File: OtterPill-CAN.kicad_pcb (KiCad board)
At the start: 2 copper layers, 30.7 x 17.6 mm, 10 parts, among them J1 pinh, J2 pinh, J3 CAN, J5 SWD, J7 PAD, U1 TJA1051T-3

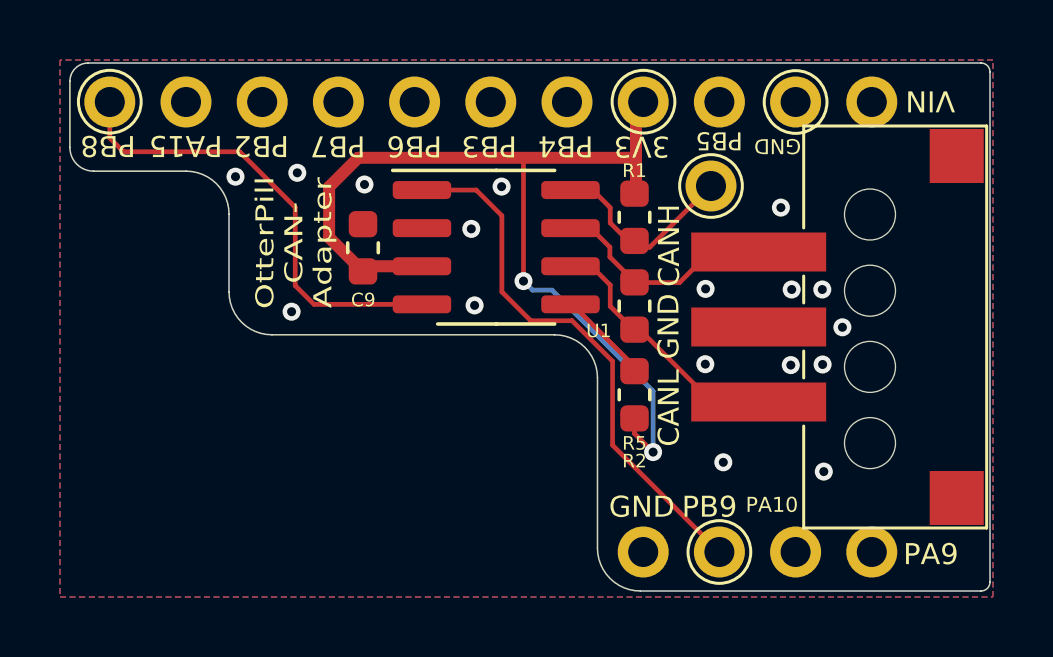
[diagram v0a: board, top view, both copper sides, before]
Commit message: updated to kicad 6
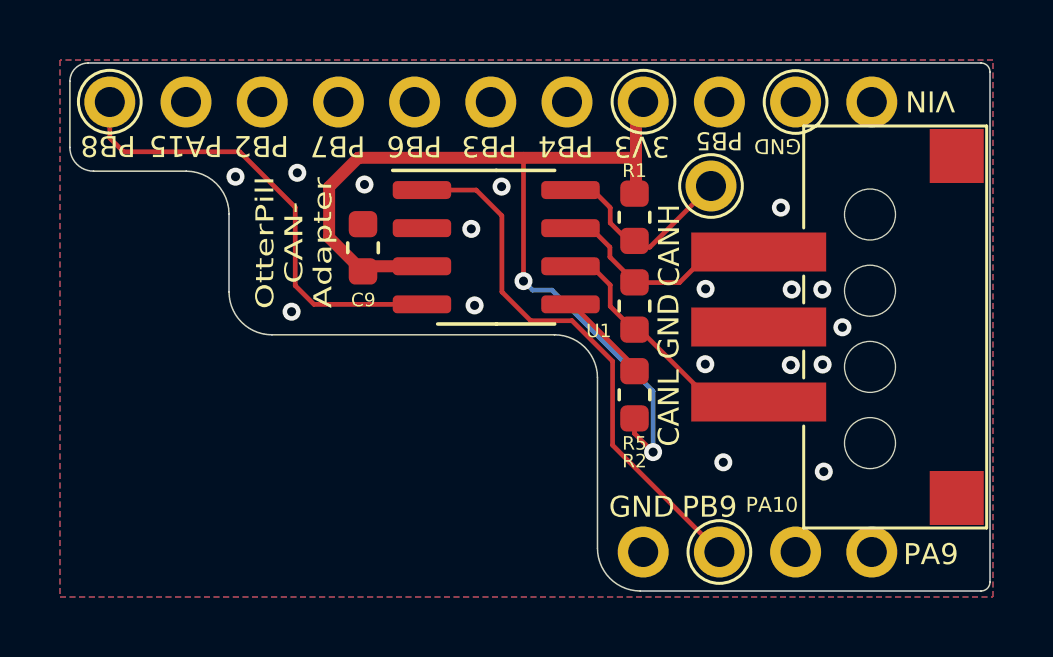
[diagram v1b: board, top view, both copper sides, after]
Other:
- net class Default removed
- net class signal removed
- board text added: "Jana Marie 2019"
- board text removed: "Jan Henrik 2019"
